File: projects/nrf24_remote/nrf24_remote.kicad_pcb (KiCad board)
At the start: 2 copper layers, 72 parts, among them J1 lipo, J2 charge, J3 mic, J4 UPDI/UART, SW1 BTN0, SW2 BTN1, SW3 BTN2, U1 MCP73831-2-OT, U2 MIC5365-3.3YC5, U3 MCP6L02x-xMS, U4 LD39020DTPU18R, U5 ATtiny1616-M, U6 LSF0102YZT, U7 74LVC2T45GT, U8 nRF24L01P, U9 LSM303AH, Y1 16MHz

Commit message: finish nnrf24_remote layout
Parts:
- C11, C13, C2, C3, C6, C9, D1, D2, D3, R1, R10, R2, R3, R4, R5, R6, R9, SW1, SW2, SW3, Y1: moved to B.Cu
- moved R19 43.1 mm to (135.2, 124.8), turned to -90 degrees
- moved R14 42.2 mm to (137.0, 113.5)
- moved C20 41.7 mm to (133.8, 123.2), turned to -90 degrees
- moved C1 41.7 mm to (138.5, 101.8), turned to -90 degrees
- moved C16 41.2 mm to (134.0, 113.5), turned to 180 degrees
- moved C26 40.5 mm to (137.0, 105.5), turned to 180 degrees
- moved C18 40.1 mm to (145.8, 122.2)
- moved R16 40.1 mm to (140.5, 105.5), turned to 180 degrees
- moved AE1 40.0 mm to (144.6, 131.4), turned to 180 degrees
- moved U4 39.8 mm to (135.0, 101.8)
- moved C25 39.0 mm to (139.0, 129.2), turned to 90 degrees
- moved C7 38.9 mm to (136.8, 101.8), turned to -90 degrees
- moved C29 37.2 mm to (134.0, 108.5), turned to 180 degrees
- moved L3 35.2 mm to (142.8, 127.0)
- moved C13 34.2 mm to (142.0, 117.0), turned to 180 degrees
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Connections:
- net Net-(C20-Pad1) renamed /XTAL-
- net Net-(C23-Pad1) renamed /XTAL+
- C16 pad 1: +3V3 -> +BATT
- U5 pad 10: /vbatt_sense -> /reg_en
- U5 pad 11: /INT1 -> /led
- U5 pad 15: /btn0 -> /btn2
- U5 pad 17: /btn2 -> /btn0
- U5 pad 18: /led -> /INT1
- U5 pad 8: /reg_en -> /mic
- U5 pad 9: /mic -> /vbatt_sense
- U7 pad 5: +3V3 -> +BATT
- U7 pad 8: +3V3 -> +BATT
- U8 pad 21: (no net) -> GND
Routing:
- net +3V3: track 0.00 -> 73.7 mm, vias 0 -> 7
- net +BATT: track 0.00 -> 54.7 mm, vias 0 -> 5
- net +1V8: track 0.00 -> 28.8 mm
- net /led: track 0.00 -> 25.8 mm, vias 0 -> 2
- net /reg_en: track 0.00 -> 21.5 mm
- net /vbatt_sense: track 0.00 -> 14.8 mm
- net /btn0: track 0.00 -> 14.2 mm, vias 0 -> 1
- net /SCL_1v8: track 0.00 -> 12.6 mm, vias 0 -> 2
- net +5V: track 0.00 -> 11.6 mm, vias 0 -> 2
- net /SDA: track 0.00 -> 11.1 mm, vias 0 -> 2
- net /dbg_tx: track 0.00 -> 10.7 mm, vias 0 -> 2
- net /INT1: track 0.00 -> 9.68 mm
- net /IRQ: track 0.00 -> 9.14 mm, vias 0 -> 2
- net /XTAL-: track 0.00 -> 8.58 mm
- net /XTAL+: track 0.00 -> 8.55 mm
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- added copper zone on B.Cu, net GND
- added copper zone on F.Cu, net GND
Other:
- board outline added: 16 x 43 mm
- board text added: "- +"
- board text added: "nrf24_remote matt tran"

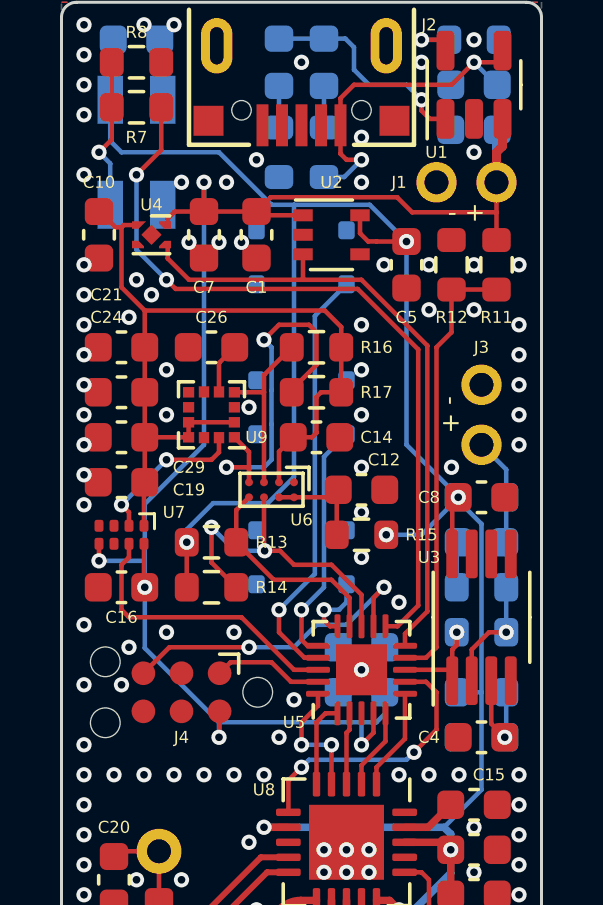
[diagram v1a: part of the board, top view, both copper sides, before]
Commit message: update nrf24_remote
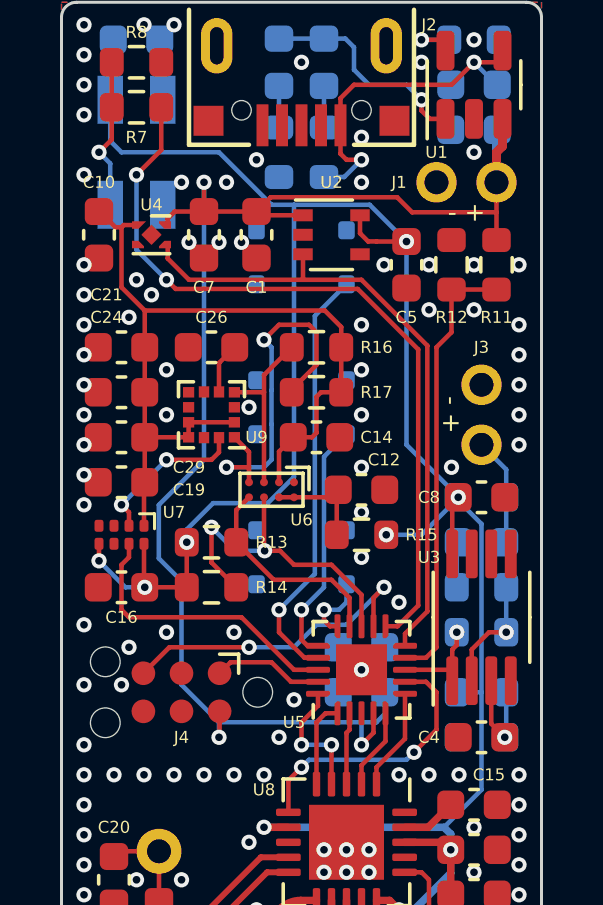
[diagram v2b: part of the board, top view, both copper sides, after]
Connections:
- C16 pad 1: +BATT -> +3V3
- U7 pad 5: +BATT -> +3V3
- U7 pad 8: +BATT -> +3V3
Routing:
- net +3V3: track 73.7 -> 79.0 mm, vias 7 -> 9
- net +BATT: track 54.7 -> 50.8 mm, vias 5 -> 3
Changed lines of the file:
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@@
       (net 1 "GND") (pinfunction "GND") (pintype "power_in"))
     (pad "5" smd roundrect (at 0.3 0.75 270) (size 0.4 0.3) (layers "F.Cu" "F.Paste" "F.Mask") (roundrect_rratio 0.25)
-      (net 2 "+BATT") (pinfunction "DIR") (pintype "input"))
+      (net 7 "+3V3") (pinfunction "DIR") (pintype "input"))
     (pad "6" smd roundrect (at 0.3 0.25 270) (size 0.4 0.3) (layers "F.Cu" "F.Paste" "F.Mask") (roundrect_rratio 0.25)
       (net 55 "unconnected-(U7-Pad6)") (pinfunction "2B") (pintype "bidirectional+no_connect"))
@@
       (net 51 "/INT1") (pinfunction "1B") (pintype "bidirectional"))
     (pad "8" smd roundrect (at 0.3 -0.75 270) (size 0.4 0.3) (layers "F.Cu" "F.Paste" "F.Mask") (roundrect_rratio 0.25)
-      (net 2 "+BATT") (pinfunction "VCCB") (pintype "power_in"))
+      (net 7 "+3V3") (pinfunction "VCCB") (pintype "power_in"))
   )
   (footprint "Inductor_SMD:L_0603_1608Metric" (layer "F.Cu")
@@
     (fp_line (start 0.8 0.4) (end -0.8 0.4) (layer "F.Fab") (width 0.1))
     (pad "1" smd roundrect (at -0.775 0 180) (size 0.9 0.95) (layers "F.Cu" "F.Paste" "F.Mask") (roundrect_rratio 0.25)
-      (net 2 "+BATT") (pintype "passive"))
+      (net 7 "+3V3") (pintype "passive"))
     (pad "2" smd roundrect (at 0.775 0 180) (size 0.9 0.95) (layers "F.Cu" "F.Paste" "F.Mask") (roundrect_rratio 0.25)
       (net 1 "GND") (pintype "passive"))
@@
   (segment (start 146.5 99) (end 146.5 100) (width 0.3) (layer "F.Cu") (net 2))
   (segment (start 142.4 118.35) (end 142 118.75) (width 0.1524) (layer "F.Cu") (net 2))
-  (segment (start 134.75 113.475) (end 134.775 113.5) (width 0.1524) (layer "F.Cu") (net 2))
   (segment (start 137.27 117.635) (end 137.27 118.48) (width 0.1524) (layer "F.Cu") (net 2))
   (segment (start 142.4 117.7) (end 142.4 118.35) (width 0.1524) (layer "F.Cu") (net 2))
-  (segment (start 134.75 112.05) (end 134.75 113.475) (width 0.1524) (layer "F.Cu") (net 2))
-  (segment (start 133.25 112.05) (end 133.25 112.6191) (width 0.1524) (layer "F.Cu") (net 2))
   (segment (start 146.7 97.8875) (end 146.7 98.8) (width 0.3) (layer "F.Cu") (net 2))
   (segment (start 138.5 100.975) (end 136.75 100.975) (width 0.1524) (layer "F.Cu") (net 2))
   (via (at 136.75 100) (size 0.508) (drill 0.254) (layers "F.Cu" "B.Cu") (net 2))
-  (via (at 133.25 112.6191) (size 0.508) (drill 0.254) (layers "F.Cu" "B.Cu") (net 2))
   (via (at 137.25 118.5) (size 0.508) (drill 0.254) (layers "F.Cu" "B.Cu") (net 2))
   (via (at 142 118.75) (size 0.508) (drill 0.254) (layers "F.Cu" "B.Cu") (net 2))
-  (via (at 134.775 113.5) (size 0.508) (drill 0.254) (layers "F.Cu" "B.Cu") (net 2))
-  (segment (start 136.75 108.75) (end 134.775 110.725) (width 0.1524) (layer "B.Cu") (net 2))
   (segment (start 146.5 100) (end 146.5 98.275) (width 0.3) (layer "B.Cu") (net 2))
   (segment (start 146.5 98.275) (end 146.525 98.25) (width 0.3) (layer "B.Cu") (net 2))
   (segment (start 142 118) (end 142.5 118) (width 0.1524) (layer "B.Cu") (net 2))
-  (segment (start 134.775 115.525) (end 137.25 118) (width 0.1524) (layer "B.Cu") (net 2))
-  (segment (start 134.775 113.5) (end 134.775 115.525) (width 0.1524) (layer "B.Cu") (net 2))
+  (segment (start 135.2449 112.537631) (end 136 113.292731) (width 0.1524) (layer "B.Cu") (net 2))
+  (segment (start 136.75 109.25) (end 135.2449 110.7551) (width 0.1524) (layer "B.Cu") (net 2))
+  (segment (start 136 116.75) (end 137.25 118) (width 0.1524) (layer "B.Cu") (net 2))
   (segment (start 142.5 118) (end 142.775 117.725) (width 0.1524) (layer "B.Cu") (net 2))
+  (segment (start 135.2449 110.7551) (end 135.2449 112.537631) (width 0.1524) (layer "B.Cu") (net 2))
   (segment (start 137.25 118) (end 142 118) (width 0.1524) (layer "B.Cu") (net 2))
   (segment (start 137.25 118.5) (end 137.25 118) (width 0.1524) (layer "B.Cu") (net 2))
-  (segment (start 134.775 112.6191) (end 133.25 112.6191) (width 0.1524) (layer "B.Cu") (net 2))
-  (segment (start 134.775 110.725) (end 134.775 113.5) (width 0.1524) (layer "B.Cu") (net 2))
   (segment (start 142.775 117) (end 142.775 115.5) (width 0.1524) (layer "B.Cu") (net 2))
-  (segment (start 136.75 100) (end 136.75 108.75) (width 0.1524) (layer "B.Cu") (net 2))
+  (segment (start 136.75 100) (end 136.75 109.25) (width 0.1524) (layer "B.Cu") (net 2))
   (segment (start 142 118) (end 142 118.75) (width 0.1524) (layer "B.Cu") (net 2))
+  (segment (start 136 113.292731) (end 136 116.75) (width 0.1524) (layer "B.Cu") (net 2))
   (segment (start 142.775 117.725) (end 142.775 117) (width 0.1524) (layer "B.Cu") (net 2))
   (segment (start 142 99.25) (end 141.5 99.25) (width 0.1524) (layer "F.Cu") (net 3))
@@
   (segment (start 143.4375 122) (end 144.725 122) (width 0.25) (layer "F.Cu") (net 7))
   (segment (start 142.5 101.9714) (end 142.5036 101.975) (width 0.1524) (layer "F.Cu") (net 7))
+  (segment (start 136.175 113.5) (end 134.775 113.5) (width 0.1524) (layer "F.Cu") (net 7))
   (segment (start 141.95 101.7) (end 142.2214 101.9714) (width 0.1524) (layer "F.Cu") (net 7))
   (segment (start 145.025 110.7) (end 145.225 110.5) (width 0.1524) (layer "F.Cu") (net 7))
@@
   (segment (start 142.9375 123.9375) (end 143.25 124.25) (width 0.25) (layer "F.Cu") (net 7))
   (segment (start 145.025 112.3875) (end 145.025 110.7) (width 0.1524) (layer "F.Cu") (net 7))
+  (segment (start 134.75 113.475) (end 134.775 113.5) (width 0.1524) (layer "F.Cu") (net 7))
+  (segment (start 134.75 112.05) (end 134.75 113.475) (width 0.1524) (layer "F.Cu") (net 7))
   (segment (start 144.725 122) (end 144.975 122.25) (width 0.25) (layer "F.Cu") (net 7))
+  (segment (start 133.25 112.05) (end 133.25 112.6191) (width 0.1524) (layer "F.Cu") (net 7))
   (segment (start 142.2214 101.9714) (end 142.5 101.9714) (width 0.1524) (layer "F.Cu") (net 7))
   (segment (start 142.5036 101.975) (end 143.5 101.975) (width 0.1524) (layer "F.Cu") (net 7))
@@
   (via (at 144.975 122.25) (size 0.508) (drill 0.254) (layers "F.Cu" "B.Cu") (net 7))
   (via (at 143.5 101.975) (size 0.508) (drill 0.254) (layers "F.Cu" "B.Cu") (net 7))
+  (via (at 133.25 112.6191) (size 0.508) (drill 0.254) (layers "F.Cu" "B.Cu") (net 7))
   (via (at 145.225 110.5) (size 0.508) (drill 0.254) (layers "F.Cu" "B.Cu") (net 7))
   (via (at 143.25 124.25) (size 0.508) (drill 0.254) (layers "F.Cu" "B.Cu") (net 7))
   (via (at 136.175 112) (size 0.508) (drill 0.254) (layers "F.Cu" "B.Cu") (net 7))
+  (via (at 134.775 113.5) (size 0.508) (drill 0.254) (layers "F.Cu" "B.Cu") (net 7))
   (via (at 138.75 121.5) (size 0.508) (drill 0.254) (layers "F.Cu" "B.Cu") (net 7))
   (via (at 142.825 111.75) (size 0.508) (drill 0.254) (layers "F.Cu" "B.Cu") (net 7))
@@
   (segment (start 146 117) (end 146 120.25) (width 0.1524) (layer "B.Cu") (net 7))
   (segment (start 137.25 99) (end 139 100.75) (width 0.1524) (layer "B.Cu") (net 7))
+  (segment (start 134.1309 113.5) (end 133.25 112.6191) (width 0.1524) (layer "B.Cu") (net 7))
   (segment (start 146 111.3875) (end 145.175 110.5625) (width 0.1524) (layer "B.Cu") (net 7))
   (segment (start 144.975 122.25) (end 144.975 121.725) (width 0.25) (layer "B.Cu") (net 7))
@@
   (segment (start 139.75 109.821452) (end 139.75 100.75) (width 0.1524) (layer "B.Cu") (net 7))
   (segment (start 144 111.75) (end 145.175 110.575) (width 0.1524) (layer "B.Cu") (net 7))
+  (segment (start 134.775 113.5) (end 134.1309 113.5) (width 0.1524) (layer "B.Cu") (net 7))
   (segment (start 143.5 108.75) (end 143.5 101.975) (width 0.1524) (layer "B.Cu") (net 7))
   (segment (start 145.175 110.425) (end 143.5 108.75) (width 0.1524) (layer "B.Cu") (net 7))

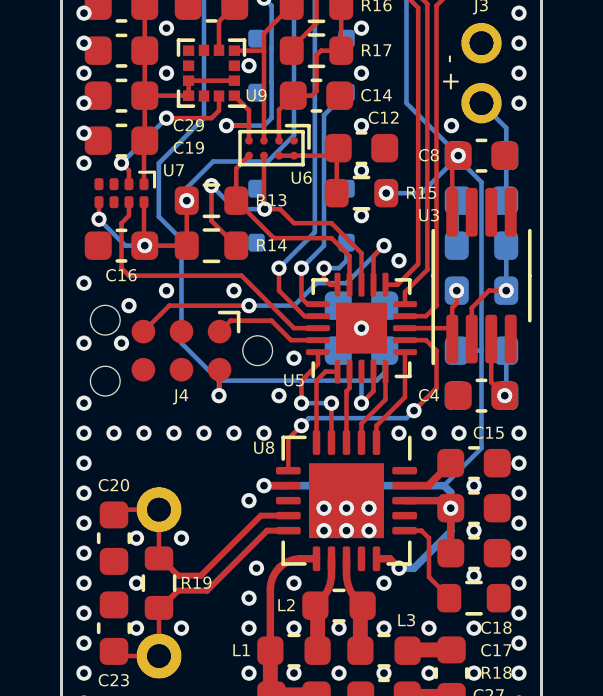
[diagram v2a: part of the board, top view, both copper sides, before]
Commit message: update nrf24_remote layout
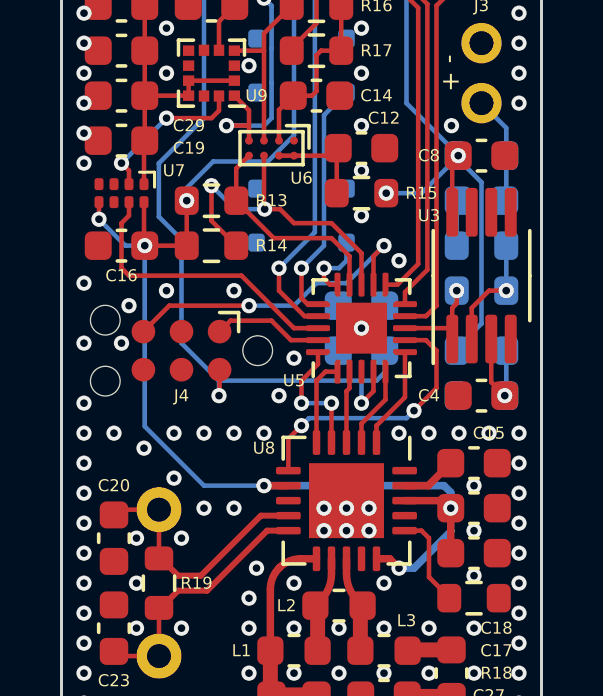
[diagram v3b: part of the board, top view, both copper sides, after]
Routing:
- net +3V3: track 79.0 -> 84.3 mm
- net GND: vias 148 -> 151
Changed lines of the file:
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@@
       (connect_pads (clearance 0))
       (min_thickness 0.254)
-      (keepout (tracks allowed) (vias not_allowed) (pads allowed ) (copperpour not_allowed) (footprints not_allowed))
+      (keepout (tracks allowed) (vias not_allowed) (pads allowed) (copperpour not_allowed) (footprints not_allowed))
       (fill (thermal_gap 0.508) (thermal_bridge_width 0.508))
       (polygon
@@
       (connect_pads (clearance 0))
       (min_thickness 0.254)
-      (keepout (tracks allowed) (vias not_allowed) (pads not_allowed ) (copperpour allowed) (footprints allowed))
+      (keepout (tracks allowed) (vias not_allowed) (pads not_allowed) (copperpour allowed) (footprints allowed))
       (fill (thermal_gap 0.508) (thermal_bridge_width 0.508))
       (polygon
@@
       (connect_pads (clearance 0))
       (min_thickness 0.254)
-      (keepout (tracks allowed) (vias not_allowed) (pads not_allowed ) (copperpour allowed) (footprints allowed))
+      (keepout (tracks allowed) (vias not_allowed) (pads not_allowed) (copperpour allowed) (footprints allowed))
       (fill (thermal_gap 0.508) (thermal_bridge_width 0.508))
       (polygon
@@
       (connect_pads (clearance 0))
       (min_thickness 0.254)
-      (keepout (tracks allowed) (vias not_allowed) (pads not_allowed ) (copperpour allowed) (footprints allowed))
+      (keepout (tracks allowed) (vias not_allowed) (pads not_allowed) (copperpour allowed) (footprints allowed))
       (fill (thermal_gap 0.508) (thermal_bridge_width 0.508))
       (polygon
@@
   (via (at 132.75 102.75) (size 0.508) (drill 0.254) (layers "F.Cu" "B.Cu") (free) (net 1))
   (via (at 135.75 94.75) (size 0.508) (drill 0.254) (layers "F.Cu" "B.Cu") (free) (net 1))
+  (via (at 136.75 122.25) (size 0.508) (drill 0.254) (layers "F.Cu" "B.Cu") (free) (net 1))
   (via (at 145.75 123) (size 0.508) (drill 0.254) (layers "F.Cu" "B.Cu") (free) (net 1))
   (via (at 142 116.25) (size 0.508) (drill 0.254) (layers "F.Cu" "B.Cu") (net 1))
@@
   (via (at 135.5 106.25) (size 0.508) (drill 0.254) (layers "F.Cu" "B.Cu") (free) (net 1))
   (via (at 138 102) (size 0.508) (drill 0.254) (layers "F.Cu" "B.Cu") (free) (net 1))
+  (via (at 134.75 120.25) (size 0.508) (drill 0.254) (layers "F.Cu" "B.Cu") (free) (net 1))
   (via (at 145.75 124.5) (size 0.508) (drill 0.254) (layers "F.Cu" "B.Cu") (free) (net 1))
   (via (at 147.25 108.75) (size 0.508) (drill 0.254) (layers "F.Cu" "B.Cu") (free) (net 1))
@@
   (via (at 138.25 129.25) (size 0.508) (drill 0.254) (layers "F.Cu" "B.Cu") (free) (net 1))
   (via (at 145.75 95.25) (size 0.508) (drill 0.254) (layers "F.Cu" "B.Cu") (free) (net 1))
+  (via (at 135.75 121.25) (size 0.508) (drill 0.254) (layers "F.Cu" "B.Cu") (free) (net 1))
   (via (at 141.75 130.75) (size 0.508) (drill 0.254) (layers "F.Cu" "B.Cu") (free) (net 1))
   (via (at 136 126.25) (size 0.508) (drill 0.254) (layers "F.Cu" "B.Cu") (free) (net 1))
@@
   (via (at 145 109.5) (size 0.508) (drill 0.254) (layers "F.Cu" "B.Cu") (free) (net 1))
   (via (at 137.75 130.75) (size 0.508) (drill 0.254) (layers "F.Cu" "B.Cu") (free) (net 1))
+  (via (at 137.75 122.25) (size 0.508) (drill 0.254) (layers "F.Cu" "B.Cu") (free) (net 1))
   (via (at 140.75 123) (size 0.508) (drill 0.254) (layers "F.Cu" "B.Cu") (net 1))
   (via (at 132.75 94.75) (size 0.508) (drill 0.254) (layers "F.Cu" "B.Cu") (free) (net 1))
   (via (at 139.75 117.25) (size 0.508) (drill 0.254) (layers "F.Cu" "B.Cu") (free) (net 1))
   (via (at 142.75 129.25) (size 0.508) (drill 0.254) (layers "F.Cu" "B.Cu") (free) (net 1))
-  (via (at 138.25 122) (size 0.508) (drill 0.254) (layers "F.Cu" "B.Cu") (free) (net 1))
   (via (at 144.25 126.25) (size 0.508) (drill 0.254) (layers "F.Cu" "B.Cu") (free) (net 1))
   (via (at 142.75 102.75) (size 0.508) (drill 0.254) (layers "F.Cu" "B.Cu") (free) (net 1))
@@
   (via (at 134.75 94.75) (size 0.508) (drill 0.254) (layers "F.Cu" "B.Cu") (free) (net 1))
   (via (at 132.75 109.75) (size 0.508) (drill 0.254) (layers "F.Cu" "B.Cu") (free) (net 1))
-  (via (at 134.75 119.75) (size 0.508) (drill 0.254) (layers "F.Cu" "B.Cu") (free) (net 1))
   (via (at 134.75 130.75) (size 0.508) (drill 0.254) (layers "F.Cu" "B.Cu") (free) (net 1))
   (via (at 137.75 115) (size 0.508) (drill 0.254) (layers "F.Cu" "B.Cu") (free) (net 1))
@@
   (via (at 141.5 122.25) (size 0.508) (drill 0.254) (layers "F.Cu" "B.Cu") (net 1))
   (via (at 140.75 130.75) (size 0.508) (drill 0.254) (layers "F.Cu" "B.Cu") (free) (net 1))
+  (via (at 146.25 119.75) (size 0.508) (drill 0.254) (layers "F.Cu" "B.Cu") (free) (net 1))
   (via (at 132.75 123.75) (size 0.508) (drill 0.254) (layers "F.Cu" "B.Cu") (free) (net 1))
   (via (at 142.25 122.25) (size 0.508) (drill 0.254) (layers "F.Cu" "B.Cu") (net 1))
@@
   (via (at 142.825 111.75) (size 0.508) (drill 0.254) (layers "F.Cu" "B.Cu") (net 7))
   (segment (start 145.175 110.5) (end 145.175 110.425) (width 0.1524) (layer "B.Cu") (net 7))
-  (segment (start 146 120.25) (end 144.75 121.5) (width 0.1524) (layer "B.Cu") (net 7))
-  (segment (start 146 117) (end 146 111.3875) (width 0.1524) (layer "B.Cu") (net 7))
+  (segment (start 146 116.1) (end 146 111.3875) (width 0.1524) (layer "B.Cu") (net 7))
+  (segment (start 145.175 116.925) (end 146 116.1) (width 0.1524) (layer "B.Cu") (net 7))
   (segment (start 133.625 97.25) (end 133.625 98.625) (width 0.1524) (layer "B.Cu") (net 7))
+  (segment (start 145.175 117) (end 145.175 116.925) (width 0.1524) (layer "B.Cu") (net 7))
   (segment (start 136.175 111.575) (end 137.0548 110.6952) (width 0.1524) (layer "B.Cu") (net 7))
   (segment (start 139 100.75) (end 139.75 100.75) (width 0.1524) (layer "B.Cu") (net 7))
   (segment (start 142.275 100.75) (end 143.5 101.975) (width 0.1524) (layer "B.Cu") (net 7))
   (segment (start 136.175 112) (end 136.175 111.575) (width 0.1524) (layer "B.Cu") (net 7))
-  (segment (start 146 117) (end 146 120.25) (width 0.1524) (layer "B.Cu") (net 7))
   (segment (start 137.25 99) (end 139 100.75) (width 0.1524) (layer "B.Cu") (net 7))
   (segment (start 134.1309 113.5) (end 133.25 112.6191) (width 0.1524) (layer "B.Cu") (net 7))
-  (segment (start 146 111.3875) (end 145.175 110.5625) (width 0.1524) (layer "B.Cu") (net 7))
+  (segment (start 136.75 121.5) (end 138.75 121.5) (width 0.1524) (layer "B.Cu") (net 7))
   (segment (start 144.975 122.25) (end 144.975 121.725) (width 0.25) (layer "B.Cu") (net 7))
   (segment (start 134 99) (end 137.25 99) (width 0.1524) (layer "B.Cu") (net 7))
   (segment (start 144.975 121.725) (end 144.75 121.5) (width 0.25) (layer "B.Cu") (net 7))
-  (segment (start 145.175 117) (end 146 117) (width 0.1524) (layer "B.Cu") (net 7))
+  (segment (start 134.775 113.5) (end 134.775 119.525) (width 0.1524) (layer "B.Cu") (net 7))
   (segment (start 144.975 123.025) (end 143.75 124.25) (width 0.25) (layer "B.Cu") (net 7))
+  (segment (start 145.175 110.5625) (end 145.175 110.5) (width 0.1524) (layer "B.Cu") (net 7))
   (segment (start 139.75 100.75) (end 142.275 100.75) (width 0.1524) (layer "B.Cu") (net 7))
   (segment (start 138.876252 110.6952) (end 139.75 109.821452) (width 0.1524) (layer "B.Cu") (net 7))
   (segment (start 133.625 95.35) (end 133.725 95.25) (width 0.1524) (layer "B.Cu") (net 7))
-  (segment (start 145.175 110.5625) (end 145.175 110.5) (width 0.1524) (layer "B.Cu") (net 7))
   (segment (start 144.975 122.25) (end 144.975 123.025) (width 0.25) (layer "B.Cu") (net 7))
   (segment (start 142.825 111.75) (end 144 111.75) (width 0.1524) (layer "B.Cu") (net 7))
+  (segment (start 134.775 119.525) (end 136.75 121.5) (width 0.1524) (layer "B.Cu") (net 7))
   (segment (start 137.0548 110.6952) (end 138.876252 110.6952) (width 0.1524) (layer "B.Cu") (net 7))
+  (segment (start 146 111.3875) (end 145.175 110.5625) (width 0.1524) (layer "B.Cu") (net 7))
   (segment (start 133.625 98.625) (end 134 99) (width 0.1524) (layer "B.Cu") (net 7))
   (segment (start 143.75 124.25) (end 143.25 124.25) (width 0.25) (layer "B.Cu") (net 7))

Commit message: update mic hpf
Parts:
- C3: value 10u -> 1u
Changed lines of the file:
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@@
       (effects (font (size 0.4 0.4) (thickness 0.1)) (justify mirror))
     )
-    (fp_text value "10u" (at 0 -1.43) (layer "B.Fab")
+    (fp_text value "1u" (at 0 -1.43) (layer "B.Fab")
       (effects (font (size 1 1) (thickness 0.15)) (justify mirror))
     )
